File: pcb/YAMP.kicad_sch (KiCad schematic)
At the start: 8 parts, among them SW1 SW_Push, SW2 SW_Push, SW3 SW_Push, SW4 SW_Push, SW5 SW_Push, SW6 SW_Push, SW7 RotaryEncoder, U1 XIAO-RP2040-DIP

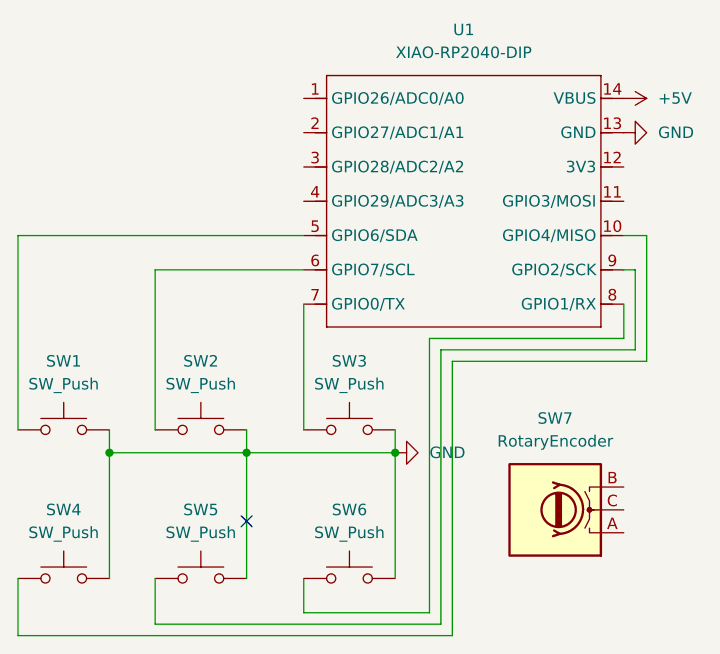
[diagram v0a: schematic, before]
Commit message: remove unused encoder from schematic file
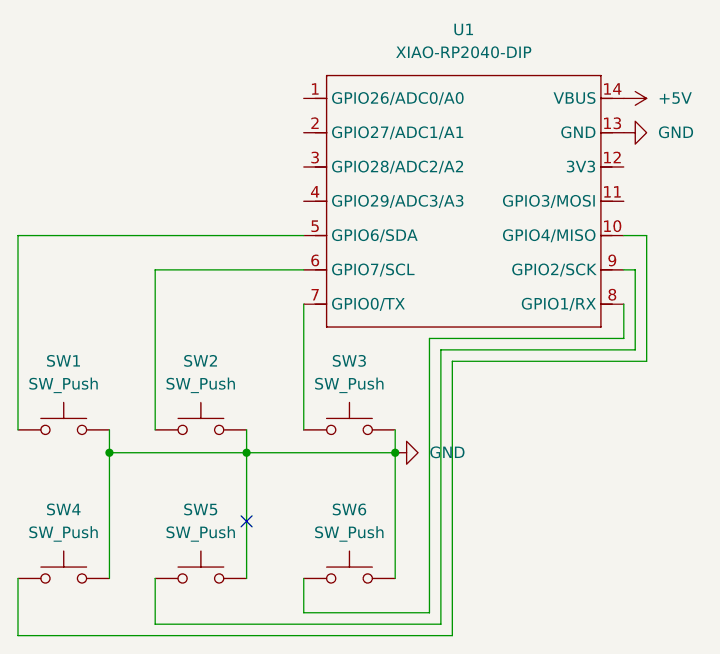
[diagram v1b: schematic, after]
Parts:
- removed SW7: RotaryEncoder, Rotary_Encoder:RotaryEncoder_Alps_EC11E_Vertical_H20mm, symbol Device:RotaryEncoder
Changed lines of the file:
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@@
-	)
-	(symbol
-		(lib_id "Device:RotaryEncoder")
-		(at 81.28 97.79 180)
-		(unit 1)
-		(exclude_from_sim no)
-		(in_bom yes)
-		(on_board yes)
-		(dnp no)
-		(fields_autoplaced yes)
-		(property "Reference" "SW7"
-			(at 81.28 87.63 0)
-			(effects
-				(font
-					(size 1.27 1.27)
-				)
-			)
-		)
-		(property "Value" "RotaryEncoder"
-			(at 81.28 90.17 0)
-			(effects
-				(font
-					(size 1.27 1.27)
-				)
-			)
-		)
-		(property "Footprint" "Rotary_Encoder:RotaryEncoder_Alps_EC11E_Vertical_H20mm"
-			(at 85.09 101.854 0)
-			(effects
-				(font
-					(size 1.27 1.27)
-				)
-				(hide yes)
-			)
-		)
-		(property "Datasheet" "~"
-			(at 81.28 104.394 0)
-			(effects
-				(font
-					(size 1.27 1.27)
-				)
-				(hide yes)
-			)
-		)
-		(property "Description" "Rotary encoder, dual channel, incremental quadrate outputs"
-			(at 81.28 97.79 0)
-			(effects
-				(font
-					(size 1.27 1.27)
-				)
-				(hide yes)
-			)
-		)
-		(pin "B"
-		)
-		(pin "C"
-		)
-		(pin "A"
-		)
-		(instances
-			(project ""
-				(path "/662f5b2f-87d9-414b-832c-00a6de8ba928"
-					(reference "SW7")
-					(unit 1)
-				)
-			)
-		)
 	)
 	(symbol
